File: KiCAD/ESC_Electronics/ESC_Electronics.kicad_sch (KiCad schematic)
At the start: 58 parts, among them J1 Batt probe, J2 CA probe, J3 Test Input BNC, J4 -1000VDC SHV, J5 RV Prob, J6 Output BNC, J7 DC Power, J8 -8V, J9 +8V, U1 CR110, U2 SiPhotodiode, U3 TL051CP, U4 UA78M08, U5 UA79M08

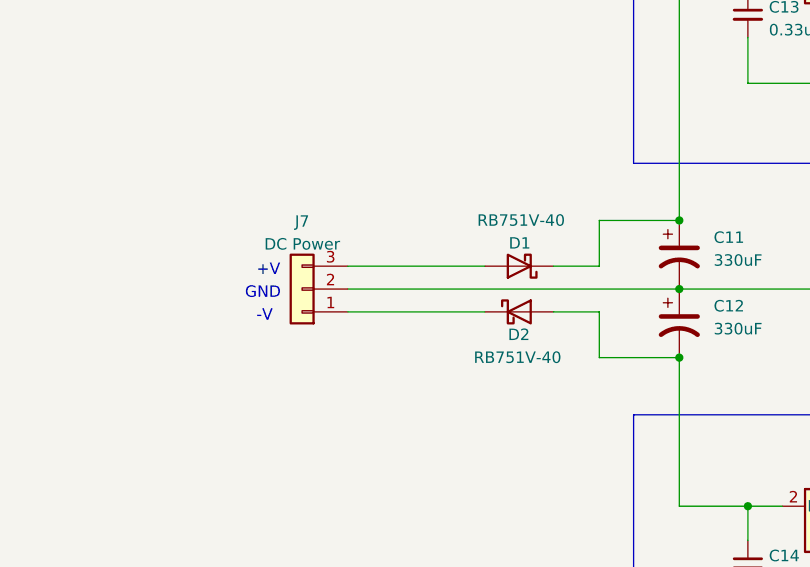
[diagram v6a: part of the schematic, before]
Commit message: added PTC to power input
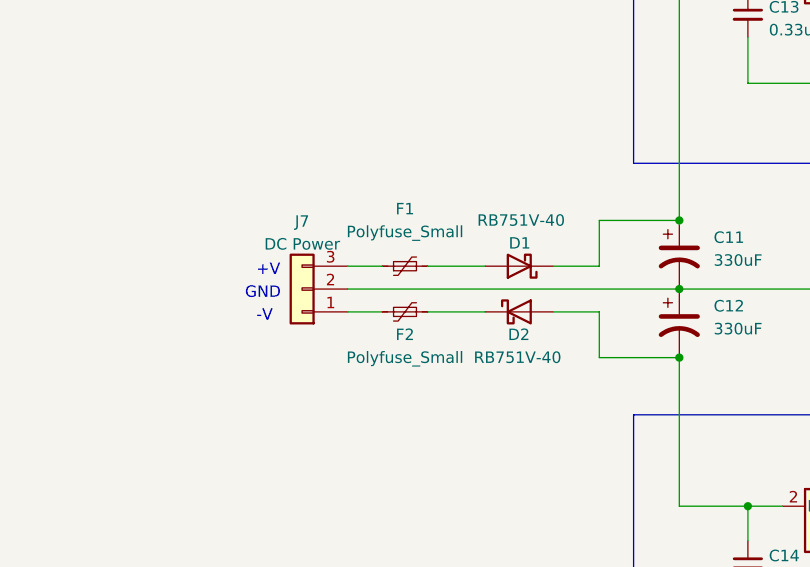
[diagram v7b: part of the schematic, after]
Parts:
- added F1, F2: Polyfuse_Small, Resistor_SMD:R_1210_3225Metric_Pad1.30x2.65mm_HandSolder, symbol Device:Polyfuse_Small
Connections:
- net at J7.1 (Pin_1): now also F2.1; no longer D2.1 (K)
- net at J7.3 (Pin_3): now also F1.1; no longer D1.2 (A)
- new net: D2.1 (K), F2.2
- new net: D1.2 (A), F1.2
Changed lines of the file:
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@@
+    (stroke (width 0) (type default))
+  )
+  (wire (pts (xy 288.29 118.11) (xy 294.64 118.11))
     (stroke (width 0) (type default))
   )
@@
     (stroke (width 0) (type default))
   )
-  (wire (pts (xy 279.4 123.19) (xy 294.64 123.19))
+  (wire (pts (xy 279.4 123.19) (xy 283.21 123.19))
     (stroke (width 0) (type default))
   )
@@
     (stroke (width 0) (type default))
   )
-  (wire (pts (xy 279.4 118.11) (xy 294.64 118.11))
+  (wire (pts (xy 279.4 118.11) (xy 283.21 118.11))
     (stroke (width 0) (type default))
   )
@@
   )
   (wire (pts (xy 344.17 97.79) (xy 335.28 97.79))
+    (stroke (width 0) (type default))
+  )
+  (wire (pts (xy 288.29 123.19) (xy 294.64 123.19))
     (stroke (width 0) (type default))
   )
@@
     )
   )
+  (symbol (lib_id "Device:Polyfuse_Small") (at 285.75 123.19 90) (unit 1)
+    (in_bom yes) (on_board yes) (dnp no)
+    (property "Reference" "F2" (at 285.75 125.73 90)
+      (effects (font (size 1.27 1.27)))
+    )
+    (property "Value" "Polyfuse_Small" (at 285.75 128.27 90)
+      (effects (font (size 1.27 1.27)))
+    )
+    (property "Footprint" "Resistor_SMD:R_1210_3225Metric_Pad1.30x2.65mm_HandSolder" (at 290.83 121.92 0)
+      (effects (font (size 1.27 1.27)) (justify left) hide)
+    )
+    (property "Datasheet" "https://www.digikey.com/en/products/detail/bel-fuse-inc/0ZCJ0010FF2E/4156128" (at 285.75 123.19 0)
+      (effects (font (size 1.27 1.27)) hide)
+    )
+    (property "Digikey" "507-1794-1-ND" (at 285.75 123.19 90)
+      (effects (font (size 1.27 1.27)) hide)
+    )
+    (pin "1")
+    (pin "2")
+    (instances
+      (project "ESC_Electronics"
+        (path "/b2dc06cf-e263-43ae-a5ba-6696795c1bac"
+          (reference "F2") (unit 1)
+        )
+      )
+    )
+  )
   (symbol (lib_id "Device:R_Small_US") (at 118.11 121.92 180) (unit 1)
     (in_bom yes) (on_board yes) (dnp no)
@@
         )
       )
+    )
+  )
+  (symbol (lib_id "Device:Polyfuse_Small") (at 285.75 118.11 90) (unit 1)
+    (in_bom yes) (on_board yes) (dnp no) (fields_autoplaced)
+    (property "Reference" "F1" (at 285.75 111.76 90)
+      (effects (font (size 1.27 1.27)))
+    )
+    (property "Value" "Polyfuse_Small" (at 285.75 114.3 90)
+      (effects (font (size 1.27 1.27)))
+    )
+    (property "Footprint" "Resistor_SMD:R_1210_3225Metric_Pad1.30x2.65mm_HandSolder" (at 290.83 116.84 0)
+      (effects (font (size 1.27 1.27)) (justify left) hide)
+    )
+    (property "Datasheet" "https://www.digikey.com/en/products/detail/bel-fuse-inc/0ZCJ0010FF2E/4156128" (at 285.75 118.11 0)
+      (effects (font (size 1.27 1.27)) hide)
+    )
+    (property "Digikey" "507-1794-1-ND" (at 285.75 118.11 90)
+      (effects (font (size 1.27 1.27)) hide)
+    )
+    (pin "1")
+    (pin "2")
+    (instances
+      (project "ESC_Electronics"
+        (path "/b2dc06cf-e263-43ae-a5ba-6696795c1bac"
+          (reference "F1") (unit 1)
+        )
+      )

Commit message: Updating Readme
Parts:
- C10, C9: Digikey 1276-1099-1-ND -> 1276-1003-1-ND
- C15, C16: Digikey 1276-2926-1-ND -> 1276-1003-1-ND
- C3, C7: Digikey 445-181696-ND -> 399-CGP1C102KNYDAAWL25-ND
- C6: Digikey 445-175513-ND -> 399-CGP1C472MNWDAAWL25-ND
- C8: Digikey 1276-1096-1-ND -> (none)
- R10: Digikey (none) -> RMCF0805FT20K0CT-ND
- R5: Digikey HVA12FA10M0 -> HVA12FA10M0CT-ND
- R9: Digikey (none) -> RMCF0805FT750RCT-ND
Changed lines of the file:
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@@
       (effects (font (size 1.27 1.27)) hide)
     )
-    (property "Datasheet" "https://www.digikey.com/en/products/detail/tdk-corporation/CK45-B3FD102KYGNA/4457522" (at 144.78 113.03 0)
-      (effects (font (size 1.27 1.27)) hide)
-    )
-    (property "Digikey" "445-181696-ND" (at 144.78 113.03 90)
+    (property "Datasheet" "https://www.digikey.com/en/products/detail/kemet/CGP1C102KNYDAAWL25/19110266" (at 144.78 113.03 0)
+      (effects (font (size 1.27 1.27)) hide)
+    )
+    (property "Digikey" "399-CGP1C102KNYDAAWL25-ND" (at 144.78 113.03 90)
       (effects (font (size 1.27 1.27)) hide)
     )
@@
       (effects (font (size 1.27 1.27)) hide)
     )
-    (property "Datasheet" "https://www.digikey.com/en/products/detail/samsung-electro-mechanics/CL21B104KACNNNC/3886757" (at 171.45 176.53 0)
-      (effects (font (size 1.27 1.27)) hide)
-    )
-    (property "Digikey" "1276-1099-1-ND" (at 171.45 176.53 0)
+    (property "Datasheet" "https://www.digikey.com/en/products/detail/samsung-electro-mechanics/CL21B104KBCNNNC/3886661" (at 171.45 176.53 0)
+      (effects (font (size 1.27 1.27)) hide)
+    )
+    (property "Digikey" "1276-1003-1-ND" (at 171.45 176.53 0)
       (effects (font (size 1.27 1.27)) hide)
     )
@@
       (effects (font (size 1.27 1.27)) hide)
     )
-    (property "Datasheet" "https://www.digikey.com/en/products/detail/samsung-electro-mechanics/CL21B105KAFNFNE/3888584" (at 344.17 151.13 0)
-      (effects (font (size 1.27 1.27)) hide)
-    )
-    (property "Digikey" "1276-2926-1-ND" (at 344.17 151.13 0)
+    (property "Datasheet" "https://www.digikey.com/en/products/detail/samsung-electro-mechanics/CL21B104KBCNNNC/3886661" (at 344.17 151.13 0)
+      (effects (font (size 1.27 1.27)) hide)
+    )
+    (property "Digikey" "1276-1003-1-ND" (at 344.17 151.13 0)
       (effects (font (size 1.27 1.27)) hide)
     )
@@
       (effects (font (size 1.27 1.27)) hide)
     )
-    (property "Datasheet" "" (at 165.1 158.75 0)
+    (property "Datasheet" "https://www.digikey.com/en/products/detail/stackpole-electronics-inc/RMCF0805FT750R/1760518" (at 165.1 158.75 0)
+      (effects (font (size 1.27 1.27)) hide)
+    )
+    (property "Digikey" "RMCF0805FT750RCT-ND" (at 165.1 158.75 0)
       (effects (font (size 1.27 1.27)) hide)
     )
@@
       (effects (font (size 1.27 1.27)) hide)
     )
-    (property "Datasheet" "https://www.digikey.com/en/products/detail/samsung-electro-mechanics/CL21A106KOQNNNE/3886754" (at 152.4 170.18 0)
-      (effects (font (size 1.27 1.27)) hide)
-    )
-    (property "Digikey" "1276-1096-1-ND" (at 152.4 170.18 0)
+    (property "Datasheet" "" (at 152.4 170.18 0)
+      (effects (font (size 1.27 1.27)) hide)
+    )
+    (property "Digikey" "" (at 152.4 170.18 0)
       (effects (font (size 1.27 1.27)) hide)
     )
@@
       (effects (font (size 1.27 1.27)) hide)
     )
-    (property "Datasheet" "https://www.digikey.com/en/products/detail/tdk-corporation/CK45-B3DD472KYNNA/7383746" (at 144.78 90.17 0)
-      (effects (font (size 1.27 1.27)) hide)
-    )
-    (property "Digikey" "445-175513-ND" (at 144.78 90.17 90)
+    (property "Datasheet" "https://www.digikey.com/en/products/detail/kemet/CGP1C472MNWDAAWL25/19110125?s=N4IgjCBcpgLFoDGUBmBDANgZwKYBoQB7KAbRADYAOAJnIGYQCwaAGAdgFZGRqw64IAXQIAHAC5QQAZTEAnAJYA7AOYgAvgQ4tKCEMkjps%2BIqR5w6O4SHGSZCleqYBOSk937DuAsUhkWIQQ0eFlg3aD1UTC8TXxBYNhYWAAIRADEA0QlIEABVRXkxAHkUAFkcNCwAV1kcRxAAWmp3KDlK4x8yLkC1NSA" (at 144.78 90.17 0)
+      (effects (font (size 1.27 1.27)) hide)
+    )
+    (property "Digikey" "399-CGP1C472MNWDAAWL25-ND" (at 144.78 90.17 90)
       (effects (font (size 1.27 1.27)) hide)
     )
@@
       (effects (font (size 1.27 1.27)) hide)
     )
-    (property "Datasheet" "https://www.digikey.com/en/products/detail/samsung-electro-mechanics/CL21B105KAFNFNE/3888584" (at 344.17 90.17 0)
-      (effects (font (size 1.27 1.27)) hide)
-    )
-    (property "Digikey" "1276-2926-1-ND" (at 344.17 90.17 0)
+    (property "Datasheet" "https://www.digikey.com/en/products/detail/samsung-electro-mechanics/CL21B104KBCNNNC/3886661" (at 344.17 90.17 0)
+      (effects (font (size 1.27 1.27)) hide)
+    )
+    (property "Digikey" "1276-1003-1-ND" (at 344.17 90.17 0)
       (effects (font (size 1.27 1.27)) hide)
     )
@@
       (effects (font (size 1.27 1.27)) hide)
     )
-    (property "Datasheet" "" (at 170.18 158.75 0)
+    (property "Datasheet" "https://www.digikey.com/en/products/detail/stackpole-electronics-inc/RMCF0805FT20K0/1760314" (at 170.18 158.75 0)
+      (effects (font (size 1.27 1.27)) hide)
+    )
+    (property "Digikey" "RMCF0805FT20K0CT-ND" (at 170.18 158.75 0)
       (effects (font (size 1.27 1.27)) hide)
     )
@@
       (effects (font (size 1.27 1.27)) hide)
     )
-    (property "Datasheet" "https://www.digikey.com/en/products/detail/tdk-corporation/CK45-B3FD102KYGNA/4457522" (at 124.46 137.16 0)
-      (effects (font (size 1.27 1.27)) hide)
-    )
-    (property "Digikey" "445-181696-ND" (at 124.46 137.16 90)
+    (property "Datasheet" "https://www.digikey.com/en/products/detail/kemet/CGP1C102KNYDAAWL25/19110266" (at 124.46 137.16 0)
+      (effects (font (size 1.27 1.27)) hide)
+    )
+    (property "Digikey" "399-CGP1C102KNYDAAWL25-ND" (at 124.46 137.16 90)
       (effects (font (size 1.27 1.27)) hide)
     )
@@
       (effects (font (size 1.27 1.27)) hide)
     )
-    (property "Datasheet" "https://www.digikey.com/en/products/detail/samsung-electro-mechanics/CL21B104KACNNNC/3886757" (at 193.04 176.53 0)
-      (effects (font (size 1.27 1.27)) hide)
-    )
-    (property "Digikey" "1276-1099-1-ND" (at 193.04 176.53 0)
+    (property "Datasheet" "https://www.digikey.com/en/products/detail/samsung-electro-mechanics/CL21B104KBCNNNC/3886661" (at 193.04 176.53 0)
+      (effects (font (size 1.27 1.27)) hide)
+    )
+    (property "Digikey" "1276-1003-1-ND" (at 193.04 176.53 0)
       (effects (font (size 1.27 1.27)) hide)
     )
@@
       (effects (font (size 1.27 1.27)) hide)
     )
-    (property "Datasheet" "https://www.digikey.com/en/products/detail/stackpole-electronics-inc/HVA12FA10M0/6195859" (at 130.81 102.87 0)
-      (effects (font (size 1.27 1.27)) hide)
-    )
-    (property "Digikey" "HVA12FA10M0" (at 130.81 102.87 90)
-      (effects (font (size 1.27 1.27)) hide)
-    )
+    (property "Datasheet" "https://www.digikey.com/en/products/detail/stackpole-electronics-inc/HVA12FA10M0/6195859?s=N4IgTCBcDaIBIDUCCBGMAxVAGAslgwgCoC0AcgCIgC6AvkA" (at 130.81 102.87 0)
+      (effects (font (size 1.27 1.27)) hide)
+    )
+    (property "Digikey" "HVA12FA10M0CT-ND" (at 130.81 102.87 90)
+      (effects (font (size 1.27 1.27)) hide)
+    )
